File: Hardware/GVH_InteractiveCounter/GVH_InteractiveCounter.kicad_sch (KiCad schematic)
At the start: 33 parts, among them J1 Molex Micro-Fit, J10 Electrode, J11 Electrode, J12 Conn_01x01, J13 Conn_01x01, J14 Conn_01x01, J15 Conn_01x01, J16 Conn_01x01, J17 Conn_01x01, J18 Conn_01x01, J19 Conn_01x01, J2 Molex Micro-Fit, J4 Electrode, J5 Electrode, J6 Electrode, J7 Electrode, J8 Electrode, J9 Electrode, U11 L7805, U13 SN74LVC2G17, U8 SN74HC165DR

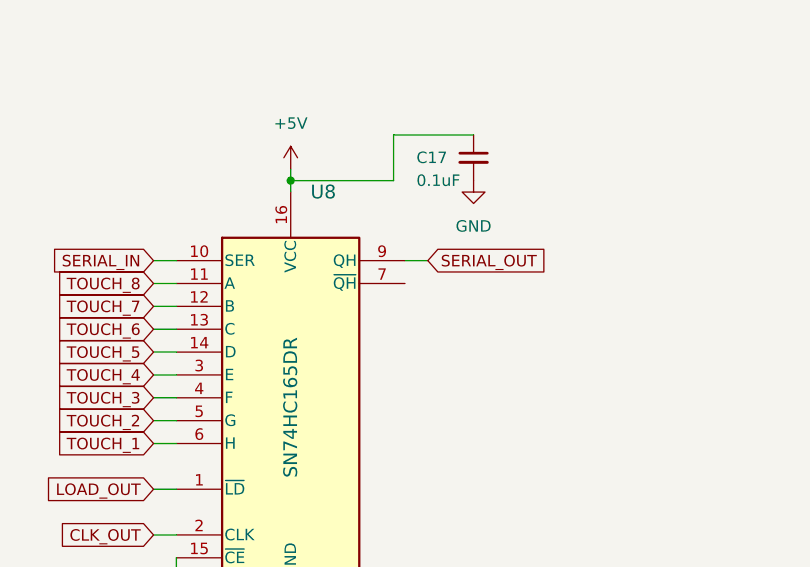
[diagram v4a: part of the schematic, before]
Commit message: Updated all of the parts to have the LCSC part numbers
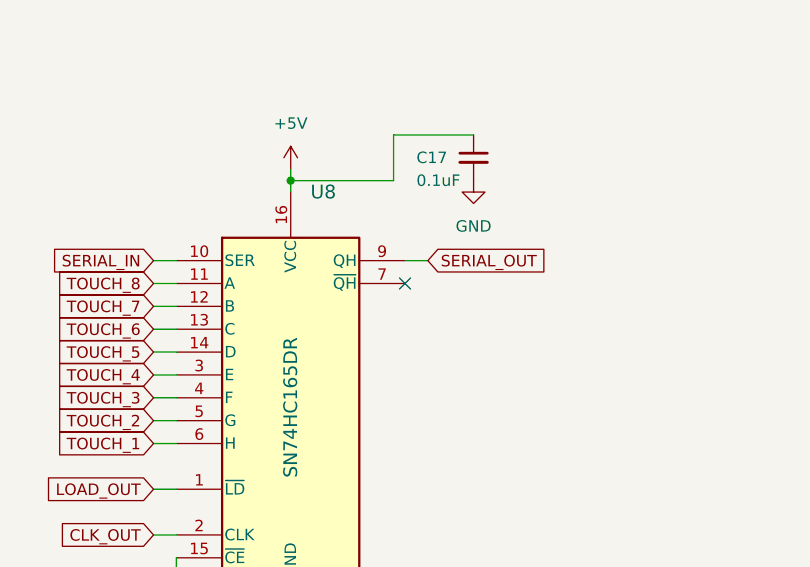
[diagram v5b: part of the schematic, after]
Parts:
- C17, C20, C22: LCSC (none) -> C15850
- C19: LCSC (none) -> C73142
- J1, J12, J2, JP11, JP14, JP15, JP16, JP17: now left out of the parts list
- R17, R18: LCSC (none) -> C17414
- U11: LCSC (none) -> C111887
- U13: Comment (none) -> SOT-23-6; LCSC (none) -> C10429; Package (none) -> SOT-23-6
- U8: footprint Package_SO:SOIC-16_3.9x9.9mm_P1.27mm -> Package_SO:SOP-16_3.9x9.9mm_P1.27mm; LCSC (none) -> C61060; Package (none) -> SOP-16
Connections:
- no-connect marks 0 -> 1
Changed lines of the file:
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@@
   (junction (at 74.93 121.92) (diameter 0) (color 0 0 0 0)
   )
+  (no_connect (at 278.13 78.74))
   (wire (pts (xy 198.12 163.83) (xy 204.47 163.83))
     (stroke (width 0) (type default))
@@
       (effects (font (size 1.27 1.27)) hide)
     )
+    (property "LCSC" "C17414" (at 114.3 156.21 90)
+      (effects (font (size 1.27 1.27)) hide)
+    )
     (pin "2")
     (pin "1")
@@
   )
   (symbol (lib_id "Jumper:SolderJumper_2_Open") (at 114.3 151.13 0) (unit 1)
-    (in_bom yes) (on_board yes) (dnp no)
+    (in_bom no) (on_board yes) (dnp no)
     (property "Reference" "JP16" (at 114.3 148.59 0)
       (effects (font (size 1.27 1.27)))
@@
       (effects (font (size 1.27 1.27)) hide)
     )
+    (property "LCSC" "C17414" (at 114.3 161.29 90)
+      (effects (font (size 1.27 1.27)) hide)
+    )
     (pin "2")
     (pin "1")
@@
   )
   (symbol (lib_id "0_connector:Molex Micro-Fit 5pos") (at 36.83 44.45 0) (mirror y) (unit 1)
-    (in_bom yes) (on_board yes) (dnp no)
+    (in_bom no) (on_board yes) (dnp no)
     (property "Reference" "J1" (at 36.83 55.88 0)
       (effects (font (size 1.27 1.27)))
@@
       (effects (font (size 1.27 1.27)) hide)
     )
+    (property "LCSC" "C10429" (at 86.36 158.75 0)
+      (effects (font (size 1.27 1.27)) hide)
+    )
+    (property "Package" "SOT-23-6" (at 86.36 158.75 0)
+      (effects (font (size 1.27 1.27)) hide)
+    )
+    (property "Comment" "SOT-23-6" (at 86.36 158.75 0)
+      (effects (font (size 1.27 1.27)) hide)
+    )
     (pin "6")
     (pin "1")
@@
       (effects (font (size 1.524 1.524)) (justify left))
     )
-    (property "Footprint" "Package_SO:SOIC-16_3.9x9.9mm_P1.27mm" (at 265.43 132.715 0)
+    (property "Footprint" "Package_SO:SOP-16_3.9x9.9mm_P1.27mm" (at 265.43 132.715 0)
       (effects (font (size 1.27 1.27) italic) hide)
     )
@@
     )
     (property "Digikey P/N" "296-8250-1-ND" (at 265.43 127.635 0)
+      (effects (font (size 1.27 1.27)) hide)
+    )
+    (property "LCSC" "C61060" (at 265.43 91.44 0)
+      (effects (font (size 1.27 1.27)) hide)
+    )
+    (property "Package" "SOP-16" (at 265.43 91.44 0)
       (effects (font (size 1.27 1.27)) hide)
     )
@@
   )
   (symbol (lib_id "Jumper:SolderJumper_3_Open") (at 54.61 166.37 270) (mirror x) (unit 1)
-    (in_bom yes) (on_board yes) (dnp no)
+    (in_bom no) (on_board yes) (dnp no)
     (property "Reference" "JP15" (at 57.15 167.64 90)
       (effects (font (size 1.27 1.27)) (justify left))
@@
   )
   (symbol (lib_id "Jumper:SolderJumper_2_Open") (at 114.3 166.37 0) (unit 1)
-    (in_bom yes) (on_board yes) (dnp no)
+    (in_bom no) (on_board yes) (dnp no)
     (property "Reference" "JP17" (at 114.3 168.91 0)
       (effects (font (size 1.27 1.27)))
@@
   )
   (symbol (lib_id "0_connector:Molex Micro-Fit 5pos") (at 367.03 39.37 0) (unit 1)
-    (in_bom yes) (on_board yes) (dnp no) (fields_autoplaced)
+    (in_bom no) (on_board yes) (dnp no) (fields_autoplaced)
     (property "Reference" "J2" (at 369.57 38.1 0)
       (effects (font (size 1.27 1.27)) (justify left))
@@
       (effects (font (size 1.27 1.27)) hide)
     )
+    (property "LCSC" "C111887" (at 74.93 111.76 0)
+      (effects (font (size 1.27 1.27)) hide)
+    )
     (pin "2")
     (pin "1")
@@
       (effects (font (size 1.27 1.27)) hide)
     )
+    (property "LCSC" "C73142" (at 63.5 116.84 0)
+      (effects (font (size 1.27 1.27)) hide)
+    )
     (pin "1")
     (pin "2")
@@
       (effects (font (size 1.27 1.27)) hide)
     )
+    (property "LCSC" "C15850" (at 285.75 64.77 0)
+      (effects (font (size 1.27 1.27)) hide)
+    )
     (pin "2")
     (pin "1")
@@
       (effects (font (size 1.27 1.27)) hide)
     )
+    (property "LCSC" "C15850" (at 71.12 148.59 0)
+      (effects (font (size 1.27 1.27)) hide)
+    )
     (pin "2")
     (pin "1")
@@
   )
   (symbol (lib_name "Conn_01x01_1") (lib_id "Connector_Generic:Conn_01x01") (at 219.71 33.02 90) (unit 1)
-    (in_bom yes) (on_board yes) (dnp no) (fields_autoplaced)
+    (in_bom no) (on_board yes) (dnp no) (fields_autoplaced)
     (property "Reference" "J12" (at 222.25 31.75 90)
       (effects (font (size 1.27 1.27)) (justify right))
@@
       (effects (font (size 1.27 1.27)) hide)
     )
+    (property "LCSC" "C15850" (at 85.09 116.84 0)
+      (effects (font (size 1.27 1.27)) hide)
+    )
     (pin "2")
     (pin "1")
@@
   )
   (symbol (lib_id "Jumper:SolderJumper_2_Open") (at 74.93 100.33 0) (unit 1)
-    (in_bom yes) (on_board yes) (dnp no)
+    (in_bom no) (on_board yes) (dnp no)
     (property "Reference" "JP11" (at 74.93 97.79 0)
       (effects (font (size 1.27 1.27)))
@@
   )
   (symbol (lib_id "Jumper:SolderJumper_3_Open") (at 54.61 151.13 270) (unit 1)
-    (in_bom yes) (on_board yes) (dnp no)
+    (in_bom no) (on_board yes) (dnp no)
     (property "Reference" "JP14" (at 57.15 149.86 90)
       (effects (font (size 1.27 1.27)) (justify left))

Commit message: Layouts done and ordered.
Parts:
- C17, C20, C22: LCSC C15850 -> C1711
- JP14, JP15: footprint Jumper:SolderJumper-3_P1.3mm_Open_RoundedPad1.0x1.5mm_NumberLabels -> Jumper:SolderJumper-3_P1.3mm_Bridged12_RoundedPad1.0x1.5mm; symbol Jumper:SolderJumper_3_Open -> Jumper:SolderJumper_3_Bridged12
- R17, R18: LCSC C17414 -> C17408
- U11: footprint Package_TO_SOT_THT:TO-220-3_Horizontal_TabDown -> Package_TO_SOT_SMD:TO-252-2; LCSC C111887 -> C310413
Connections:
- net at JP16.1 (A), R17.2, U13.6 (1Y): now also JP14.3 (B); no longer JP14.1 (A)
- net at JP17.1 (A), R18.2, U13.4 (2Y): now also JP15.3 (B); no longer JP15.1 (A)
- net at U13.1 (1A): now also JP14.1 (A); no longer JP14.3 (B)
- net at U13.3 (2A): now also JP15.1 (A); no longer JP15.3 (B)
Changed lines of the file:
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@@
   )
   (no_connect (at 278.13 78.74))
+  (wire (pts (xy 46.99 144.78) (xy 58.42 144.78))
+    (stroke (width 0) (type default))
+  )
   (wire (pts (xy 198.12 163.83) (xy 204.47 163.83))
     (stroke (width 0) (type default))
@@
     (stroke (width 0) (type default))
   )
+  (wire (pts (xy 46.99 166.37) (xy 46.99 172.72))
+    (stroke (width 0) (type default))
+  )
   (wire (pts (xy 105.41 138.43) (xy 105.41 156.21))
     (stroke (width 0) (type default))
@@
     (stroke (width 0) (type default))
   )
+  (wire (pts (xy 58.42 144.78) (xy 58.42 151.13))
+    (stroke (width 0) (type default))
+  )
   (wire (pts (xy 92.71 100.33) (xy 92.71 99.06))
     (stroke (width 0) (type default))
@@
     (stroke (width 0) (type default))
   )
+  (wire (pts (xy 58.42 172.72) (xy 58.42 166.37))
+    (stroke (width 0) (type default))
+  )
   (wire (pts (xy 110.49 161.29) (xy 111.76 161.29))
     (stroke (width 0) (type default))
@@
     (stroke (width 0) (type default))
   )
+  (wire (pts (xy 46.99 172.72) (xy 58.42 172.72))
+    (stroke (width 0) (type default))
+  )
   (wire (pts (xy 250.19 101.6) (xy 252.73 101.6))
     (stroke (width 0) (type default))
@@
   )
   (wire (pts (xy 250.19 96.52) (xy 252.73 96.52))
+    (stroke (width 0) (type default))
+  )
+  (wire (pts (xy 46.99 151.13) (xy 46.99 144.78))
     (stroke (width 0) (type default))
   )
@@
     (effects (font (size 1.27 1.27)) (justify left bottom))
   )
-  (global_label "~{LOAD}" (shape input) (at 50.8 166.37 180) (fields_autoplaced)
+  (global_label "~{LOAD}" (shape input) (at 46.99 166.37 180) (fields_autoplaced)
     (effects (font (size 1.27 1.27)) (justify right))
-    (property "Intersheetrefs" "${INTERSHEET_REFS}" (at 43.0976 166.37 0)
+    (property "Intersheetrefs" "${INTERSHEET_REFS}" (at 39.2876 166.37 0)
       (effects (font (size 1.27 1.27)) (justify right) hide)
     )
@@
     )
   )
-  (global_label "CLK" (shape input) (at 50.8 151.13 180) (fields_autoplaced)
+  (global_label "CLK" (shape input) (at 46.99 151.13 180) (fields_autoplaced)
     (effects (font (size 1.27 1.27)) (justify right))
-    (property "Intersheetrefs" "${INTERSHEET_REFS}" (at 44.2467 151.13 0)
+    (property "Intersheetrefs" "${INTERSHEET_REFS}" (at 40.4367 151.13 0)
       (effects (font (size 1.27 1.27)) (justify right) hide)
     )
@@
       (effects (font (size 1.27 1.27)) hide)
     )
-    (property "LCSC" "C17414" (at 114.3 156.21 90)
+    (property "LCSC" "C17408" (at 114.3 156.21 90)
       (effects (font (size 1.27 1.27)) hide)
     )
@@
       (effects (font (size 1.27 1.27)) hide)
     )
-    (property "LCSC" "C17414" (at 114.3 161.29 90)
+    (property "LCSC" "C17408" (at 114.3 161.29 90)
       (effects (font (size 1.27 1.27)) hide)
     )
@@
     )
   )
-  (symbol (lib_id "Jumper:SolderJumper_3_Open") (at 54.61 166.37 270) (mirror x) (unit 1)
+  (symbol (lib_id "Jumper:SolderJumper_3_Bridged12") (at 54.61 166.37 90) (mirror x) (unit 1)
     (in_bom no) (on_board yes) (dnp no)
-    (property "Reference" "JP15" (at 57.15 167.64 90)
+    (property "Reference" "JP15" (at 52.07 165.1 90)
       (effects (font (size 1.27 1.27)) (justify left))
     )
-    (property "Value" "SolderJumper_3_Bridged12" (at 57.15 163.83 90)
+    (property "Value" "SolderJumper_3_Bridged12" (at 52.07 168.91 90)
       (effects (font (size 1.27 1.27)) (justify left) hide)
     )
-    (property "Footprint" "Jumper:SolderJumper-3_P1.3mm_Open_RoundedPad1.0x1.5mm_NumberLabels" (at 54.61 166.37 0)
+    (property "Footprint" "Jumper:SolderJumper-3_P1.3mm_Bridged12_RoundedPad1.0x1.5mm" (at 54.61 166.37 0)
       (effects (font (size 1.27 1.27)) hide)
     )
@@
       (effects (font (size 1.27 1.27)))
     )
-    (property "Footprint" "Package_TO_SOT_THT:TO-220-3_Horizontal_TabDown" (at 75.565 115.57 0)
+    (property "Footprint" "Package_TO_SOT_SMD:TO-252-2" (at 75.565 115.57 0)
       (effects (font (size 1.27 1.27) italic) (justify left) hide)
     )
@@
       (effects (font (size 1.27 1.27)) hide)
     )
-    (property "LCSC" "C111887" (at 74.93 111.76 0)
+    (property "LCSC" "C310413" (at 74.93 111.76 0)
       (effects (font (size 1.27 1.27)) hide)
     )
@@
       (effects (font (size 1.27 1.27)) hide)
     )
-    (property "LCSC" "C15850" (at 285.75 64.77 0)
+    (property "LCSC" "C1711" (at 285.75 64.77 0)
       (effects (font (size 1.27 1.27)) hide)
     )
@@
       (effects (font (size 1.27 1.27)) hide)
     )
-    (property "LCSC" "C15850" (at 71.12 148.59 0)
+    (property "LCSC" "C1711" (at 71.12 148.59 0)
       (effects (font (size 1.27 1.27)) hide)
     )
@@
       (effects (font (size 1.27 1.27)) hide)
     )
-    (property "LCSC" "C15850" (at 85.09 116.84 0)
+    (property "LCSC" "C1711" (at 85.09 116.84 0)
       (effects (font (size 1.27 1.27)) hide)
     )
@@
     )
   )
-  (symbol (lib_id "Jumper:SolderJumper_3_Open") (at 54.61 151.13 270) (unit 1)
+  (symbol (lib_id "Jumper:SolderJumper_3_Bridged12") (at 54.61 151.13 90) (unit 1)
     (in_bom no) (on_board yes) (dnp no)
-    (property "Reference" "JP14" (at 57.15 149.86 90)
+    (property "Reference" "JP14" (at 52.07 152.4 90)
       (effects (font (size 1.27 1.27)) (justify left))
     )
-    (property "Value" "SolderJumper_3_Bridged12" (at 57.15 152.4 90)
+    (property "Value" "SolderJumper_3_Bridged12" (at 52.07 149.86 90)
       (effects (font (size 1.27 1.27)) (justify left) hide)
     )
-    (property "Footprint" "Jumper:SolderJumper-3_P1.3mm_Open_RoundedPad1.0x1.5mm_NumberLabels" (at 54.61 151.13 0)
-      (effects (font (size 1.27 1.27)) hide)
-    )
+    (property "Footprint" "Jumper:SolderJumper-3_P1.3mm_Bridged12_RoundedPad1.0x1.5mm" (at 54.61 151.13 0)
+      (effects (font (size 1.27 1.27)) hide)
+    )
